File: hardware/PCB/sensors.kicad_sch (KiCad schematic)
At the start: 30 parts, among them IC1 BNO085, IC2 IIS2MDCTR, J1 IMU_EXT, J2 GPS, U6 LSM6DSOXTR, U7 BME280, U8 INA219BxDCN, U9 INA219BxDCN, Y1 Crystal

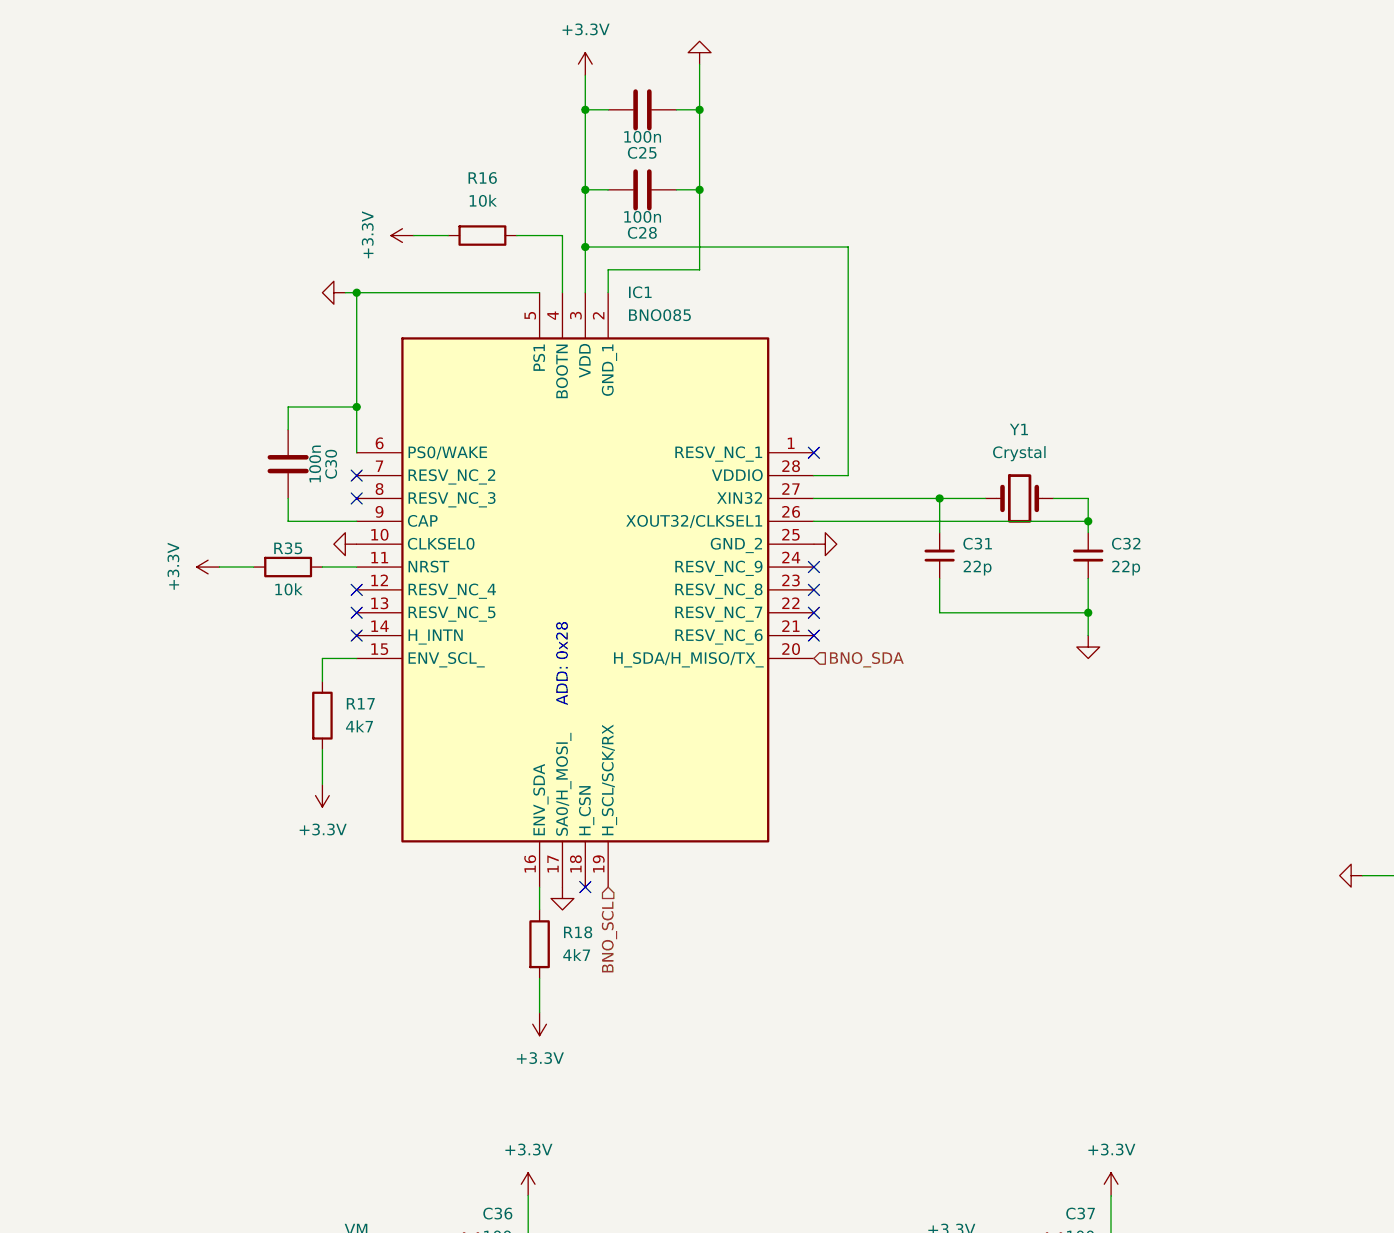
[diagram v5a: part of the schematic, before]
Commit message: Removed on-PCB BNO085 and added VL53L4CD ToF sensor
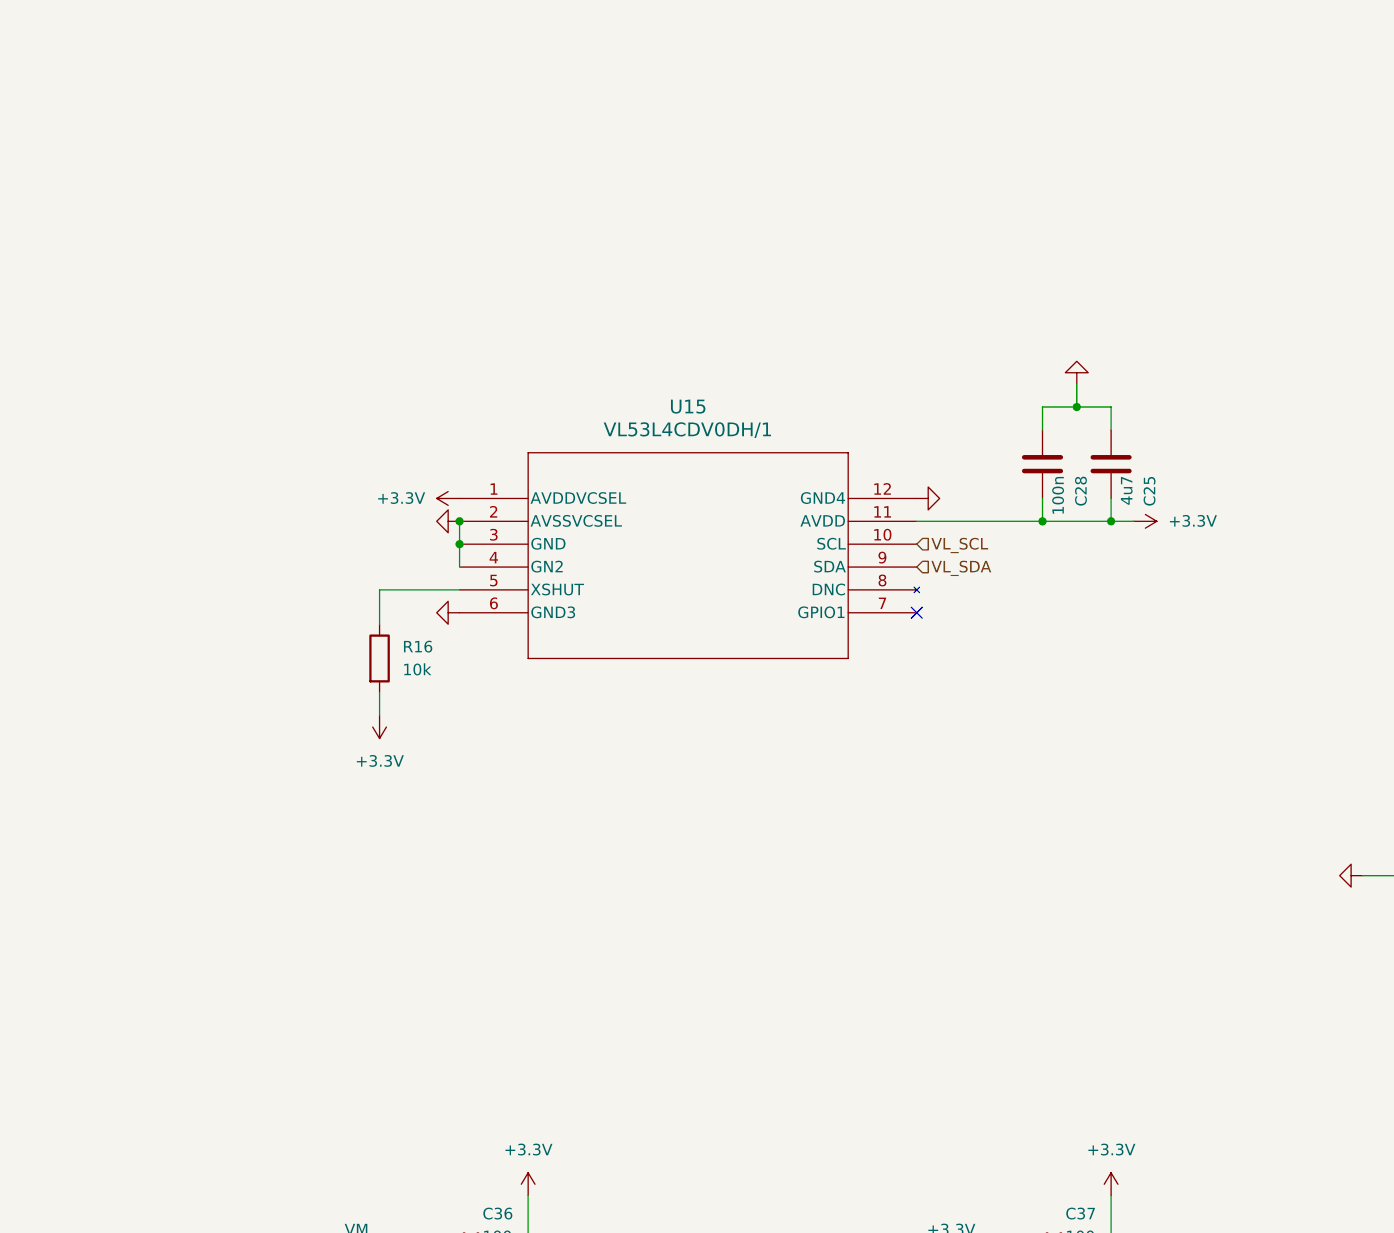
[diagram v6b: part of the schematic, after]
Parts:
- removed C30: 100n, Capacitor_SMD:C_1206_3216Metric_Pad1.33x1.80mm_HandSolder, symbol Device:C
- removed C31, C32: 22p, Capacitor_SMD:C_1206_3216Metric_Pad1.33x1.80mm_HandSolder, symbol Device:C_Small
- removed IC1: BNO085, BNO085:BNO085, symbol BNO085:BNO085
- removed R17, R18: 4k7, Capacitor_SMD:C_1206_3216Metric_Pad1.33x1.80mm_HandSolder, symbol Device:R
- removed R35: 10k, Capacitor_SMD:C_1206_3216Metric_Pad1.33x1.80mm_HandSolder, symbol Device:R
- removed Y1: Crystal, Crystal:Crystal_SMD_MicroCrystal_CC7V-T1A-2Pin_3.2x1.5mm, symbol Device:Crystal
- added U15: VL53L4CDV0DH/1, LGA12_STM, symbol 2026-03-19_11-19-21:VL53L4CDV0DH_1
- C25: value 100n -> 4u7
- R16: footprint Capacitor_SMD:C_1206_3216Metric_Pad1.33x1.80mm_HandSolder -> Resistor_SMD:R_1020_2550Metric_Pad1.33x5.20mm_HandSolder
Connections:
- net +3.3V: now also U15.1 (AVDDVCSEL), U15.11 (AVDD)
- net GND: now also U15.12 (GND4), U15.2 (AVSSVCSEL), U15.3 (GND), U15.4 (GN2), U15.6 (GND3)
- net at R16.1: now also U15.5 (XSHUT)
- new net VL_SCL: U15.10 (SCL)
- new net VL_SDA: U15.9 (SDA)
- no-connect marks 19 -> 9
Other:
- note removed: "ADD: 0x28"

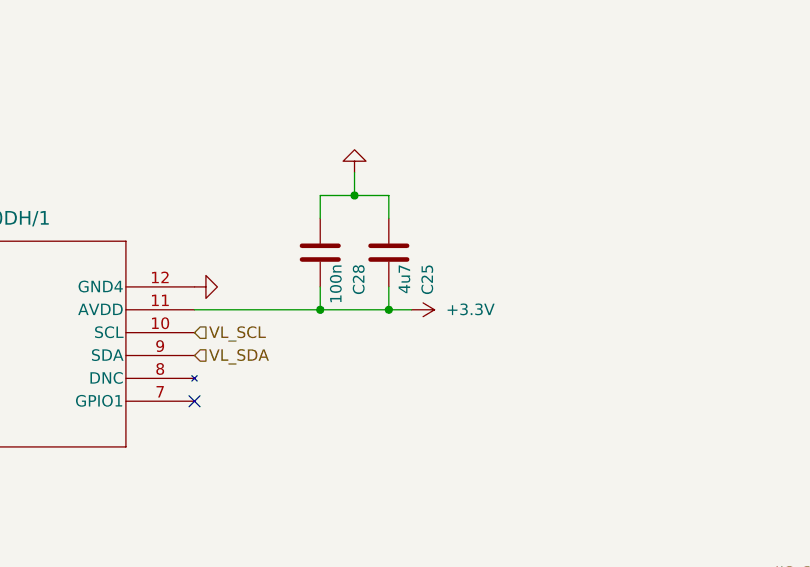
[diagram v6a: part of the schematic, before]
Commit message: Routed VL53L4CD
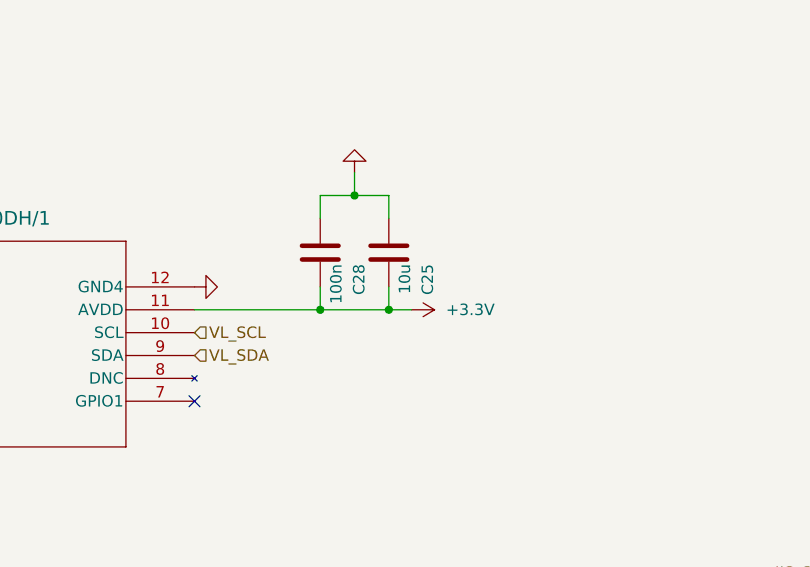
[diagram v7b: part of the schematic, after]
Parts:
- C25: value 4u7 -> 10u; footprint Capacitor_SMD:C_1206_3216Metric_Pad1.33x1.80mm_HandSolder -> Capacitor_SMD:C_1210_3225Metric_Pad1.33x2.70mm_HandSolder
- R16: footprint Resistor_SMD:R_1020_2550Metric_Pad1.33x5.20mm_HandSolder -> Resistor_SMD:R_1206_3216Metric_Pad1.30x1.75mm_HandSolder
- U15: footprint LGA12_STM -> footprints:LGA12_STM
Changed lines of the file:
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@@
 			)
 		)
-		(property "Value" "4u7"
+		(property "Value" "10u"
 			(at 137.668 66.04 90)
 			(effects
@@
 			)
 		)
-		(property "Footprint" "Capacitor_SMD:C_1206_3216Metric_Pad1.33x1.80mm_HandSolder"
+		(property "Footprint" "Capacitor_SMD:C_1210_3225Metric_Pad1.33x2.70mm_HandSolder"
 			(at 136.8552 68.58 0)
 			(effects
@@
 			)
 		)
-		(property "Footprint" "Resistor_SMD:R_1020_2550Metric_Pad1.33x5.20mm_HandSolder"
+		(property "Footprint" "Resistor_SMD:R_1206_3216Metric_Pad1.30x1.75mm_HandSolder"
 			(at 52.832 86.36 90)
 			(effects
@@
 			)
 		)
-		(property "Footprint" "LGA12_STM"
+		(property "Footprint" "footprints:LGA12_STM"
 			(at 63.5 68.58 0)
 			(effects

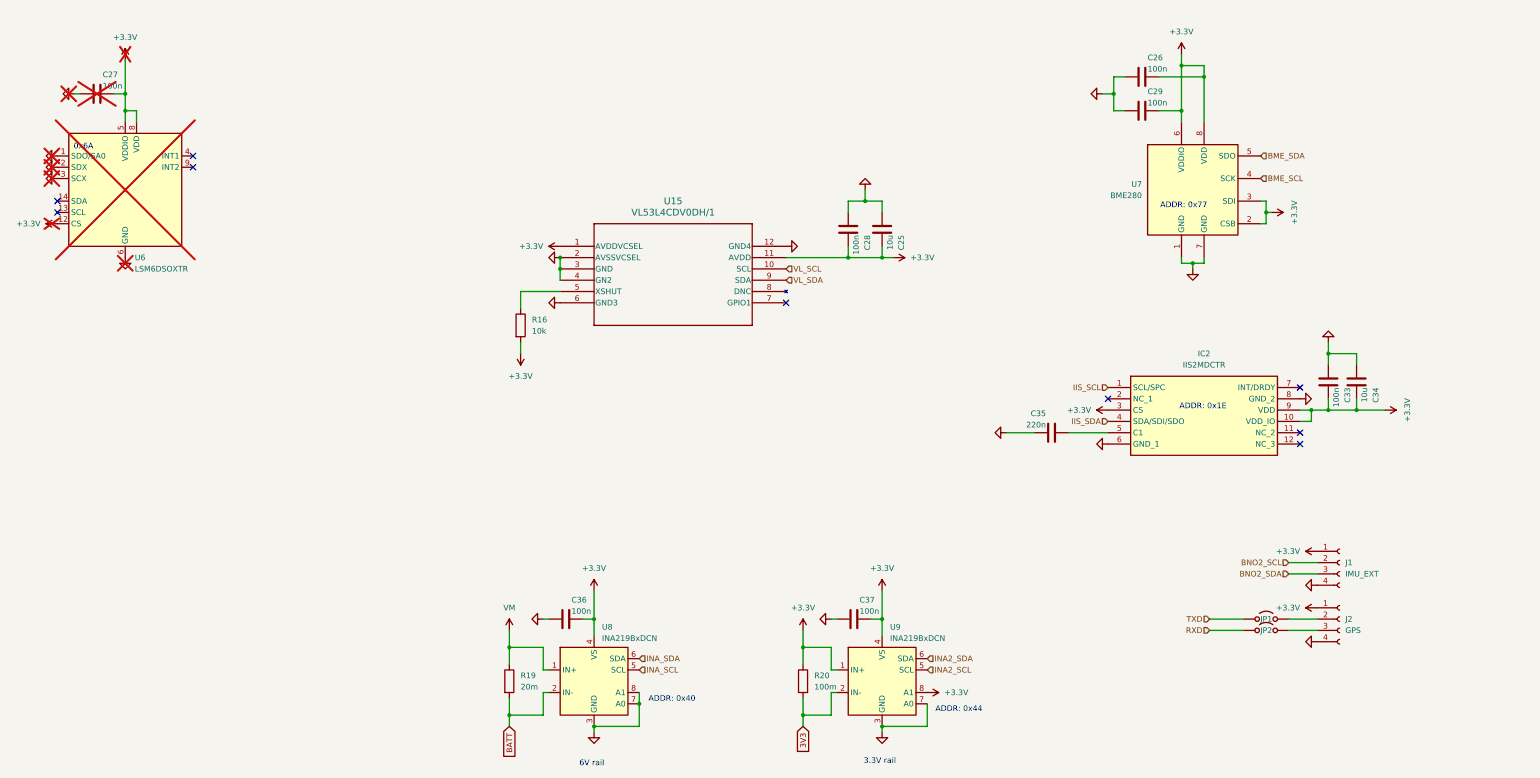
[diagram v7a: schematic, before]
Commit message: added external ToF instead of on-PCB
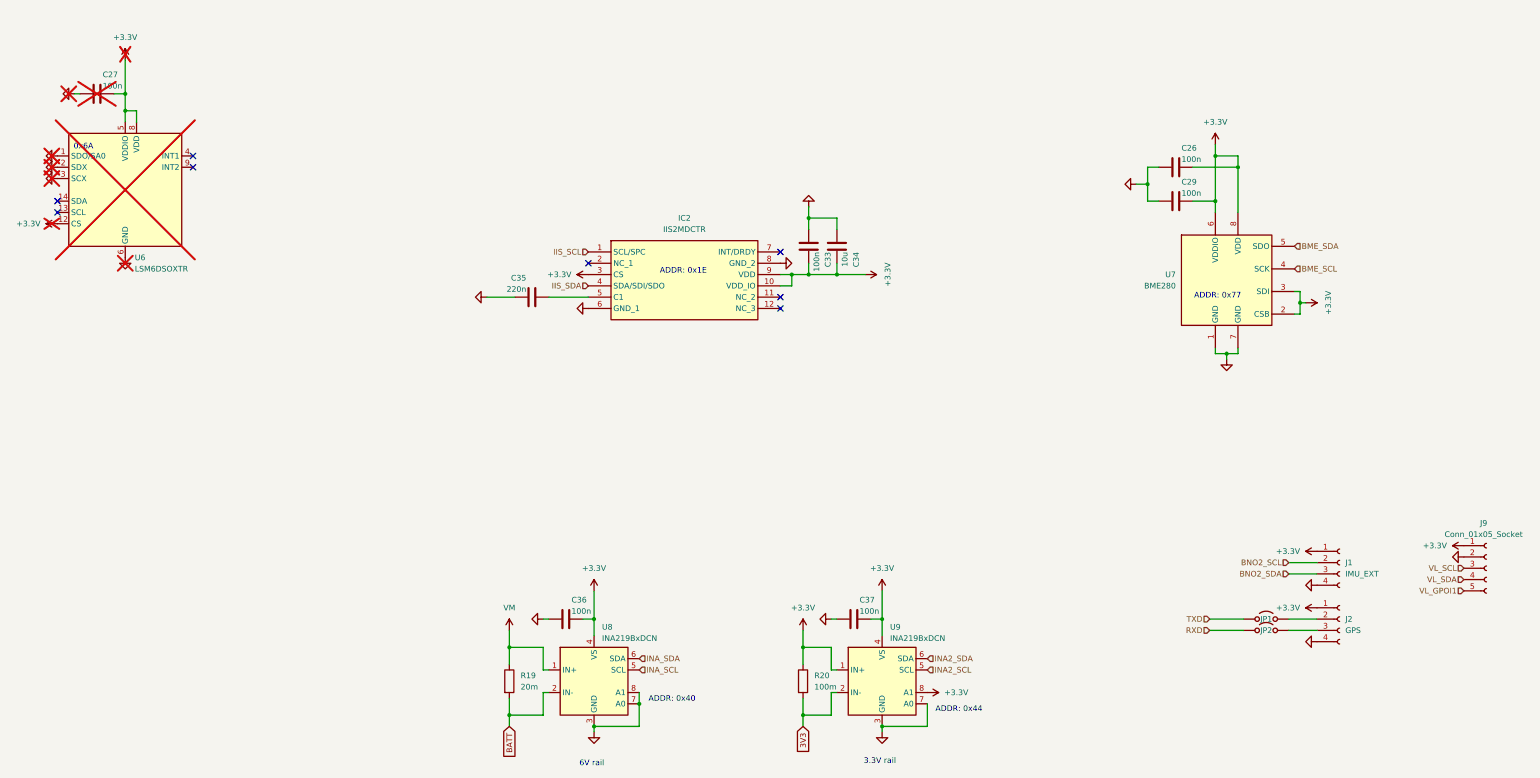
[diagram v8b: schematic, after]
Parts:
- removed C25: 10u, Capacitor_SMD:C_1210_3225Metric_Pad1.33x2.70mm_HandSolder, symbol Device:C
- removed C28: 100n, Capacitor_SMD:C_1206_3216Metric_Pad1.33x1.80mm_HandSolder, symbol Device:C
- removed R16: 10k, Resistor_SMD:R_1206_3216Metric_Pad1.30x1.75mm_HandSolder, symbol Device:R
- removed U15: VL53L4CDV0DH/1, footprints:LGA12_STM, symbol 2026-03-19_11-19-21:VL53L4CDV0DH_1
- added J9: Conn_01x05_Socket, Connector_PinSocket_2.54mm:PinSocket_1x05_P2.54mm_Vertical, symbol Connector:Conn_01x05_Socket
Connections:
- net +3.3V: now also J9.1 (Pin_1)
- net GND: now also J9.2 (Pin_2)
- net VL_SCL: now also J9.3 (Pin_3)
- net VL_SDA: now also J9.4 (Pin_4)
- new net VL_GPOI1: J9.5 (Pin_5)
- no-connect marks 9 -> 8
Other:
- moved on the sheet: C26, C29, C33, C34, C35, IC2, U7
